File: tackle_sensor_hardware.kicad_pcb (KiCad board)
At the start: 2 copper layers, 50.8 x 50.8 mm, 21 parts, among them J1 Conn_01x02_Male, J2 Conn_01x04_Male, J3 Conn_01x02_Male, Q1 DMP4051LK3, Q2 2N7002K, Q3 2N7002K, Q4 2N7002K, U1 LIS2DE12, U2 STM32G031Fx, U3 LM3488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

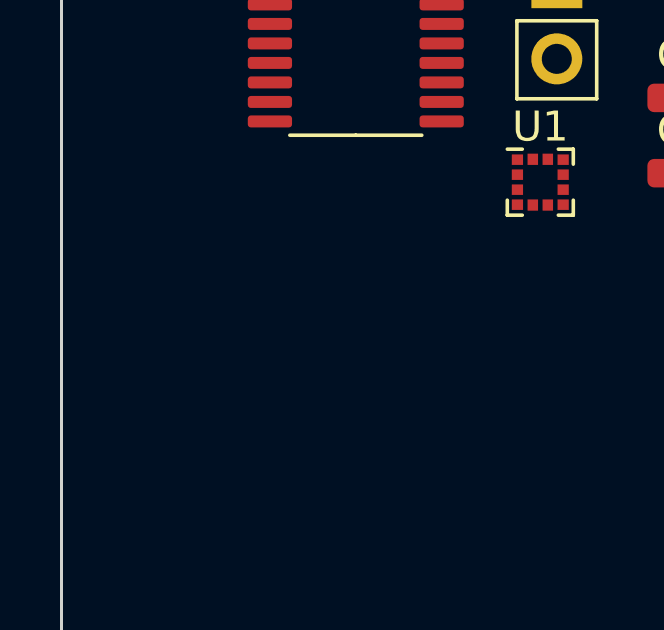
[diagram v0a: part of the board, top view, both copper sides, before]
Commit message: (WIP) added prog header to schematic and added some WIP notes.
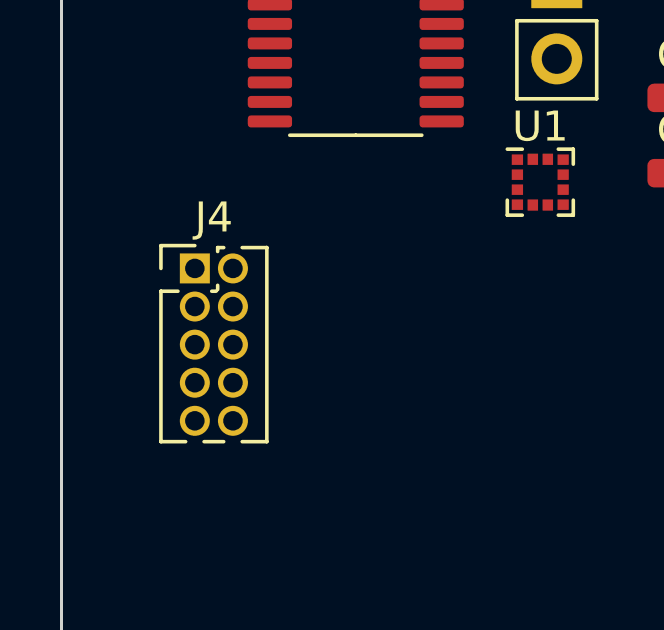
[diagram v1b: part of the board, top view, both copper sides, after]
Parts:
- added J4: Conn_ARM_JTAG_SWD_10, Connector_PinHeader_1.27mm:PinHeader_2x05_P1.27mm_Vertical, F.Cu at (125.1, 98.4)
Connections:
- U2 pad 18: unconnected-(U2-Pad18) -> /SWDIO
- U2 pad 19: unconnected-(U2-Pad19) -> /SWCLK
- U2 pad 6: unconnected-(U2-Pad6) -> /RST

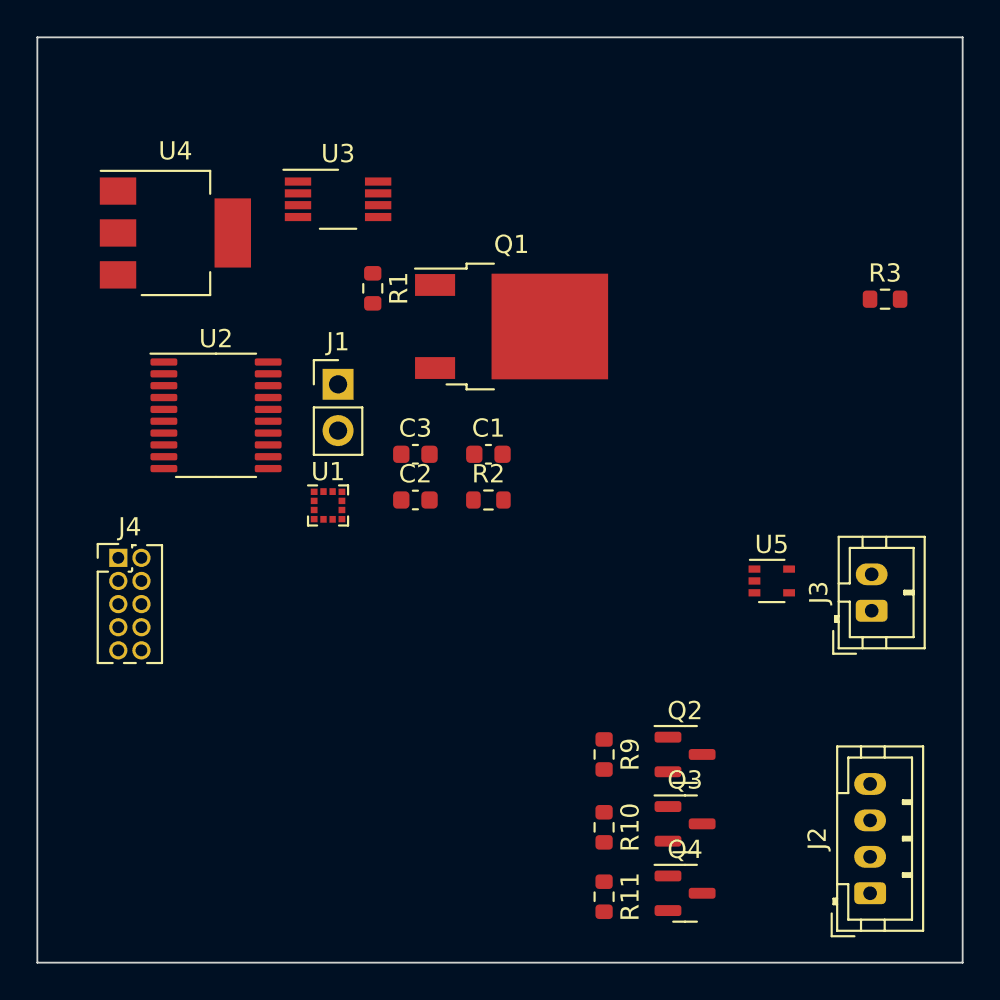
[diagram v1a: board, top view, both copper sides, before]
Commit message: added mounting holes
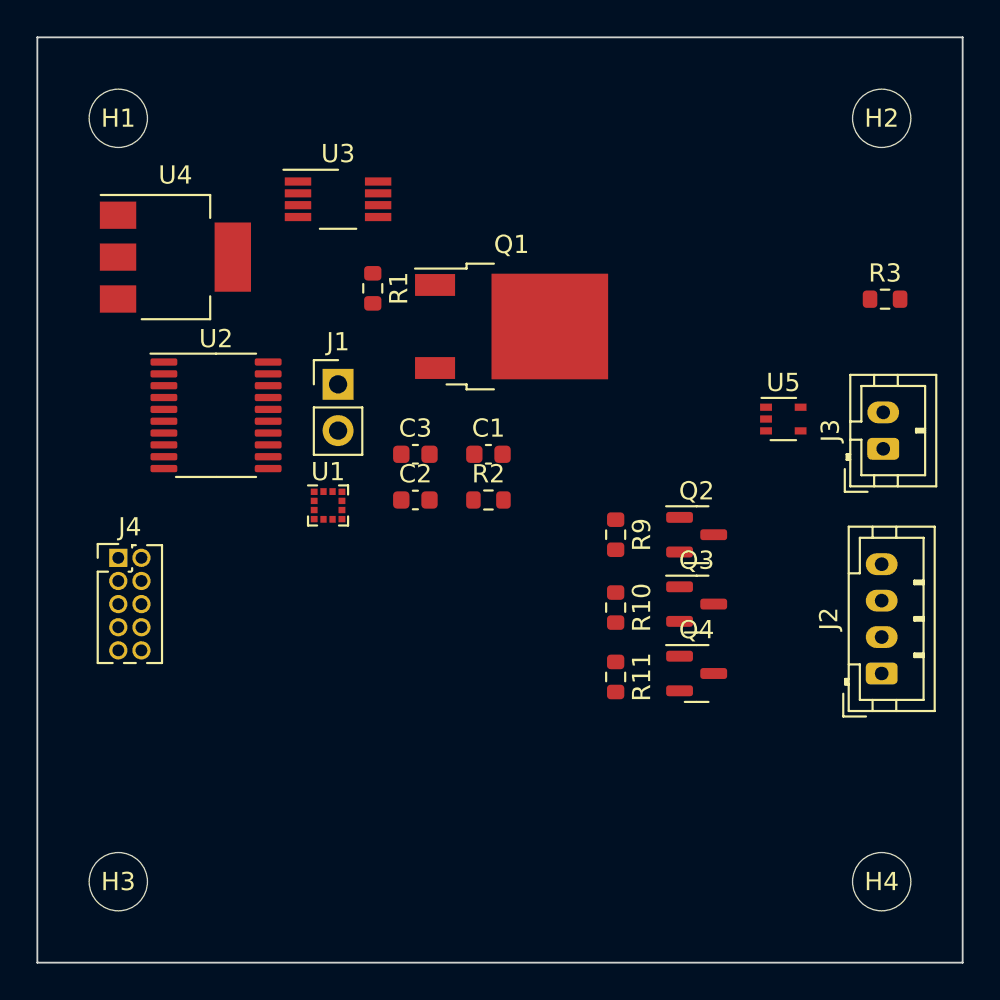
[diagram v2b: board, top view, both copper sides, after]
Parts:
- added H1: MountingHole, MountingHole:MountingHole_3.2mm_M3, F.Cu at (125.1, 74.3)
- added H2: MountingHole, MountingHole:MountingHole_3.2mm_M3, F.Cu at (167.0, 74.3)
- added H3: MountingHole, MountingHole:MountingHole_3.2mm_M3, F.Cu at (125.1, 116.2)
- added H4: MountingHole, MountingHole:MountingHole_3.2mm_M3, F.Cu at (167.0, 116.2)
- moved R10 12.1 mm to (152.4, 101.2)
- moved R11 12.1 mm to (152.4, 105.0)
- moved R9 12.1 mm to (152.4, 97.2)
- moved J2 12.1 mm to (167.0, 104.8)
- moved Q2 12.1 mm to (156.8, 97.2)
- moved Q3 12.1 mm to (156.8, 101.0)
- moved Q4 12.1 mm to (156.8, 104.8)
- moved J3 8.91 mm to (167.1, 92.4)
- moved U5 8.91 mm to (161.6, 90.8)
- moved U4 1.33 mm to (128.2, 81.9)
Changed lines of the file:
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@@
     )
+  )
+  (footprint "MountingHole:MountingHole_3.2mm_M3" (layer "F.Cu")
+    (at 125.095 116.205)
+    (descr "Mounting Hole 3.2mm, no annular, M3")
+    (tags "mounting hole 3.2mm no annular m3")
+    (property "Sheetfile" "tackle_sensor_hardware.kicad_sch")
+    (property "Sheetname" "")
+    (attr exclude_from_pos_files)
+    (fp_text reference "H3" (at 0 0) (layer "F.SilkS")
+      (effects (font (size 1 1) (thickness 0.15)))
+    )
+    (fp_text value "MountingHole" (at 0 4.2) (layer "F.Fab")
+      (effects (font (size 1 1) (thickness 0.15)))
+    )
+    (fp_text user "${REFERENCE}" (at 0.3 0) (layer "F.Fab")
+      (effects (font (size 1 1) (thickness 0.15)))
+    )
+    (fp_circle (center 0 0) (end 3.2 0) (layer "Cmts.User") (width 0.15) (fill none))
+    (fp_circle (center 0 0) (end 3.45 0) (layer "F.CrtYd") (width 0.05) (fill none))
+    (pad "" np_thru_hole circle (at 0 0) (size 3.2 3.2) (drill 3.2) (layers *.Cu *.Mask))
   )
   (footprint "Connector_JST:JST_PH_B4B-PH-K_1x04_P2.00mm_Vertical" (layer "F.Cu")
-    (at 166.37 116.84 90)
+    (at 167.005 104.775 90)
     (descr "JST PH series connector, B4B-PH-K (http://www.jst-mfg.com/product/pdf/eng/ePH.pdf), generated with kicad-footprint-generator")
     (tags "connector JST PH side entry")
@@
     )
   )
+  (footprint "MountingHole:MountingHole_3.2mm_M3" (layer "F.Cu")
+    (at 167.005 116.205)
+    (descr "Mounting Hole 3.2mm, no annular, M3")
+    (tags "mounting hole 3.2mm no annular m3")
+    (property "Sheetfile" "tackle_sensor_hardware.kicad_sch")
+    (property "Sheetname" "")
+    (attr exclude_from_pos_files)
+    (fp_text reference "H4" (at 0 0) (layer "F.SilkS")
+      (effects (font (size 1 1) (thickness 0.15)))
+    )
+    (fp_text value "MountingHole" (at 0 4.2) (layer "F.Fab")
+      (effects (font (size 1 1) (thickness 0.15)))
+    )
+    (fp_text user "${REFERENCE}" (at 0.3 0) (layer "F.Fab")
+      (effects (font (size 1 1) (thickness 0.15)))
+    )
+    (fp_circle (center 0 0) (end 3.2 0) (layer "Cmts.User") (width 0.15) (fill none))
+    (fp_circle (center 0 0) (end 3.45 0) (layer "F.CrtYd") (width 0.05) (fill none))
+    (pad "" np_thru_hole circle (at 0 0) (size 3.2 3.2) (drill 3.2) (layers *.Cu *.Mask))
+  )
   (footprint "Package_TO_SOT_SMD:SOT-23" (layer "F.Cu")
-    (at 156.21 113.03)
+    (at 156.845 100.965)
     (descr "SOT, 3 Pin (https://www.jedec.org/system/files/docs/to-236h.pdf variant AB), generated with kicad-footprint-generator ipc_gullwing_generator.py")
     (tags "SOT TO_SOT_SMD")
@@
   )
   (footprint "Package_TO_SOT_SMD:SOT-23" (layer "F.Cu")
-    (at 156.21 109.22)
+    (at 156.845 97.155)
     (descr "SOT, 3 Pin (https://www.jedec.org/system/files/docs/to-236h.pdf variant AB), generated with kicad-footprint-generator ipc_gullwing_generator.py")
     (tags "SOT TO_SOT_SMD")
@@
   )
   (footprint "Connector_JST:JST_PH_B2B-PH-K_1x02_P2.00mm_Vertical" (layer "F.Cu")
-    (at 166.455 101.33 90)
+    (at 167.09 92.44 90)
     (descr "JST PH series connector, B2B-PH-K (http://www.jst-mfg.com/product/pdf/eng/ePH.pdf), generated with kicad-footprint-generator")
     (tags "connector JST PH side entry")
@@
   )
   (footprint "Resistor_SMD:R_0603_1608Metric" (layer "F.Cu")
-    (at 151.765 117.03 -90)
+    (at 152.4 104.965 -90)
     (descr "Resistor SMD 0603 (1608 Metric), square (rectangular) end terminal, IPC_7351 nominal, (Body size source: IPC-SM-782 page 72, https://www.pcb-3d.com/wordpress/wp-content/uploads/ipc-sm-782a_amendment_1_and_2.pdf), generated with kicad-footprint-generator")
     (tags "resistor")
@@
   )
   (footprint "Resistor_SMD:R_0603_1608Metric" (layer "F.Cu")
-    (at 151.765 109.22 -90)
+    (at 152.4 97.155 -90)
     (descr "Resistor SMD 0603 (1608 Metric), square (rectangular) end terminal, IPC_7351 nominal, (Body size source: IPC-SM-782 page 72, https://www.pcb-3d.com/wordpress/wp-content/uploads/ipc-sm-782a_amendment_1_and_2.pdf), generated with kicad-footprint-generator")
     (tags "resistor")
@@
   )
   (footprint "Package_TO_SOT_SMD:SOT-353_SC-70-5" (layer "F.Cu")
-    (at 160.97 99.695)
+    (at 161.605 90.805)
     (descr "SOT-353, SC-70-5")
     (tags "SOT-353 SC-70-5")
@@
   )
   (footprint "Package_TO_SOT_SMD:SOT-223-3_TabPin2" (layer "F.Cu")
-    (at 128.23 80.59)
+    (at 128.23 81.915)
     (descr "module CMS SOT223 4 pins")
     (tags "CMS SOT")
@@
     )
   )
+  (footprint "MountingHole:MountingHole_3.2mm_M3" (layer "F.Cu")
+    (at 167.005 74.295)
+    (descr "Mounting Hole 3.2mm, no annular, M3")
+    (tags "mounting hole 3.2mm no annular m3")
+    (property "Sheetfile" "tackle_sensor_hardware.kicad_sch")
+    (property "Sheetname" "")
+    (attr exclude_from_pos_files)
+    (fp_text reference "H2" (at 0 0) (layer "F.SilkS")
+      (effects (font (size 1 1) (thickness 0.15)))
+    )
+    (fp_text value "MountingHole" (at 0 4.2) (layer "F.Fab")
+      (effects (font (size 1 1) (thickness 0.15)))
+    )
+    (fp_text user "${REFERENCE}" (at 0.3 0) (layer "F.Fab")
+      (effects (font (size 1 1) (thickness 0.15)))
+    )
+    (fp_circle (center 0 0) (end 3.2 0) (layer "Cmts.User") (width 0.15) (fill none))
+    (fp_circle (center 0 0) (end 3.45 0) (layer "F.CrtYd") (width 0.05) (fill none))
+    (pad "" np_thru_hole circle (at 0 0) (size 3.2 3.2) (drill 3.2) (layers *.Cu *.Mask))
+  )
   (footprint "Resistor_SMD:R_0603_1608Metric" (layer "F.Cu")
-    (at 151.765 113.22 -90)
+    (at 152.4 101.155 -90)
     (descr "Resistor SMD 0603 (1608 Metric), square (rectangular) end terminal, IPC_7351 nominal, (Body size source: IPC-SM-782 page 72, https://www.pcb-3d.com/wordpress/wp-content/uploads/ipc-sm-782a_amendment_1_and_2.pdf), generated with kicad-footprint-generator")
     (tags "resistor")
@@
     )
   )
+  (footprint "MountingHole:MountingHole_3.2mm_M3" (layer "F.Cu")
+    (at 125.095 74.295)
+    (descr "Mounting Hole 3.2mm, no annular, M3")
+    (tags "mounting hole 3.2mm no annular m3")
+    (property "Sheetfile" "tackle_sensor_hardware.kicad_sch")
+    (property "Sheetname" "")
+    (attr exclude_from_pos_files)
+    (fp_text reference "H1" (at 0 0) (layer "F.SilkS")
+      (effects (font (size 1 1) (thickness 0.15)))
+    )
+    (fp_text value "MountingHole" (at 0 4.2) (layer "F.Fab")
+      (effects (font (size 1 1) (thickness 0.15)))
+    )
+    (fp_text user "${REFERENCE}" (at 0.3 0) (layer "F.Fab")
+      (effects (font (size 1 1) (thickness 0.15)))
+    )
+    (fp_circle (center 0 0) (end 3.2 0) (layer "Cmts.User") (width 0.15) (fill none))
+    (fp_circle (center 0 0) (end 3.45 0) (layer "F.CrtYd") (width 0.05) (fill none))
+    (pad "" np_thru_hole circle (at 0 0) (size 3.2 3.2) (drill 3.2) (layers *.Cu *.Mask))
+  )
   (footprint "Package_TO_SOT_SMD:SOT-23" (layer "F.Cu")
-    (at 156.21 116.84)
+    (at 156.845 104.775)
     (descr "SOT, 3 Pin (https://www.jedec.org/system/files/docs/to-236h.pdf variant AB), generated with kicad-footprint-generator ipc_gullwing_generator.py")
     (tags "SOT TO_SOT_SMD")

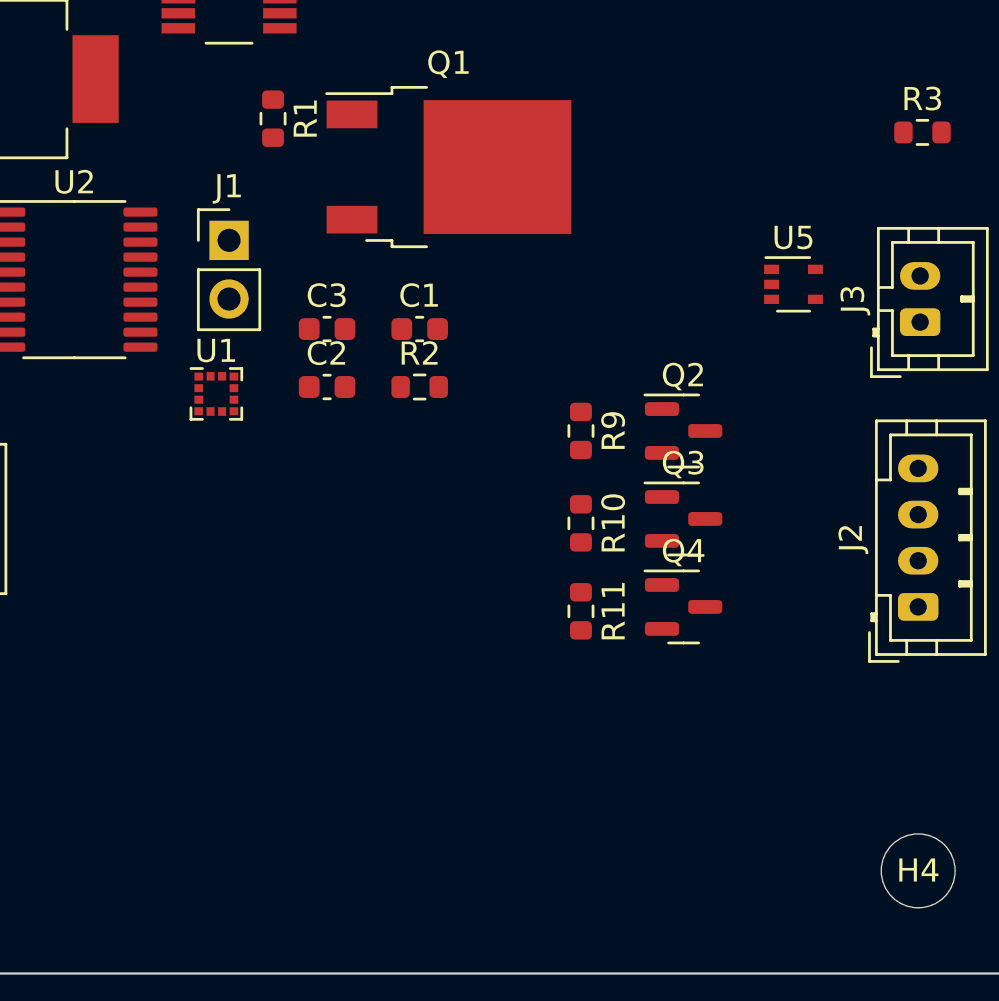
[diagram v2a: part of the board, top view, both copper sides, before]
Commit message: added on-board LEDs
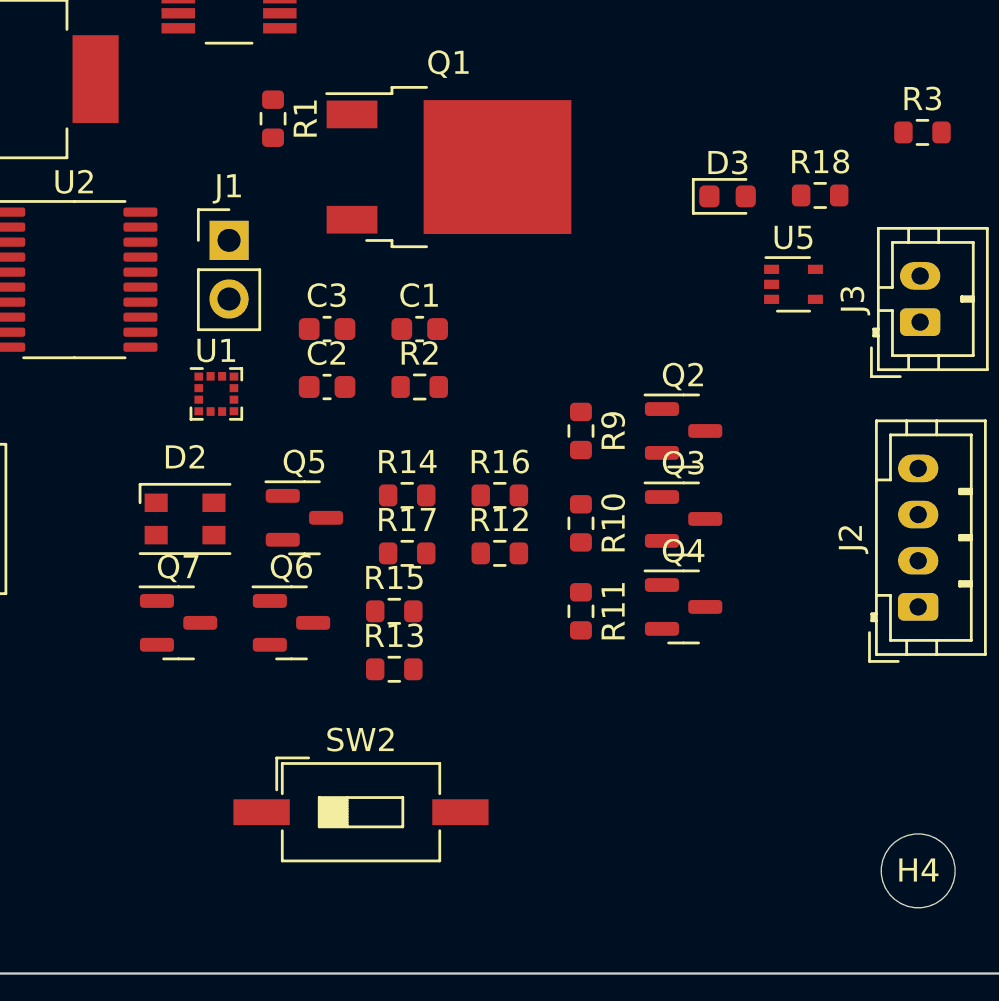
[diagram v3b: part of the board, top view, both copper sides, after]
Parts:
- added D2: CLV1A-FKB-CK1VW1DE1BB7C3C3, LED_SMD:LED_Cree-PLCC4_3.2x2.8mm_CCW, F.Cu at (135.3, 101.0)
- added D3: LED, LED_SMD:LED_0603_1608Metric, F.Cu at (158.8, 87.0)
- added Q5: 2N7002K, Package_TO_SOT_SMD:SOT-23, F.Cu at (140.4, 100.9)
- added Q6: 2N7002K, Package_TO_SOT_SMD:SOT-23, F.Cu at (139.9, 105.5)
- added Q7: 2N7002K, Package_TO_SOT_SMD:SOT-23, F.Cu at (135.0, 105.5)
- added R12: 10k, Resistor_SMD:R_0603_1608Metric, F.Cu at (148.9, 102.5)
- added R13: 1k, Resistor_SMD:R_0603_1608Metric, F.Cu at (144.3, 107.5)
- added R14: 10k, Resistor_SMD:R_0603_1608Metric, F.Cu at (144.9, 99.9)
- added R15: 1k, Resistor_SMD:R_0603_1608Metric, F.Cu at (144.3, 105.0)
- added R16: 10k, Resistor_SMD:R_0603_1608Metric, F.Cu at (148.9, 99.9)
- added R17: 1k, Resistor_SMD:R_0603_1608Metric, F.Cu at (144.9, 102.5)
- added R18: 1k, Resistor_SMD:R_0603_1608Metric, F.Cu at (162.8, 87.0)
- added SW2: SW_DIP_x01, Button_Switch_SMD:SW_DIP_SPSTx01_Slide_6.7x4.1mm_W8.61mm_P2.54mm_LowProfile, F.Cu at (142.9, 113.7)
